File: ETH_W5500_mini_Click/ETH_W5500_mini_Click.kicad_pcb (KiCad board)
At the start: 2 copper layers, 25.4 x 42.9 mm, 8 parts, among them J1 ETH W5500 mini Click v1.0, M1 W5500-MINI

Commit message: project files updated to Kicad version 9.0.1
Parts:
- J1: value ETH W5500 mini Click v1.0 -> ETH W5500 mini Click v${REVISION}

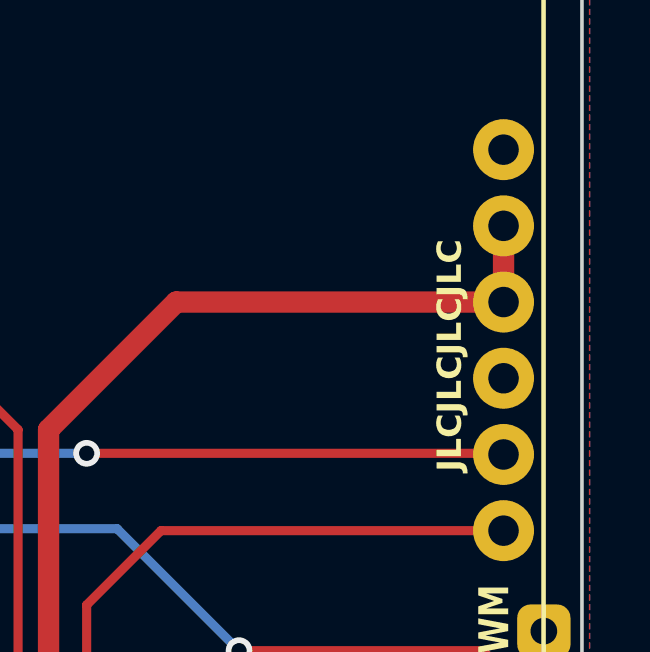
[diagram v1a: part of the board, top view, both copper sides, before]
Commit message: updated 3D models and project files
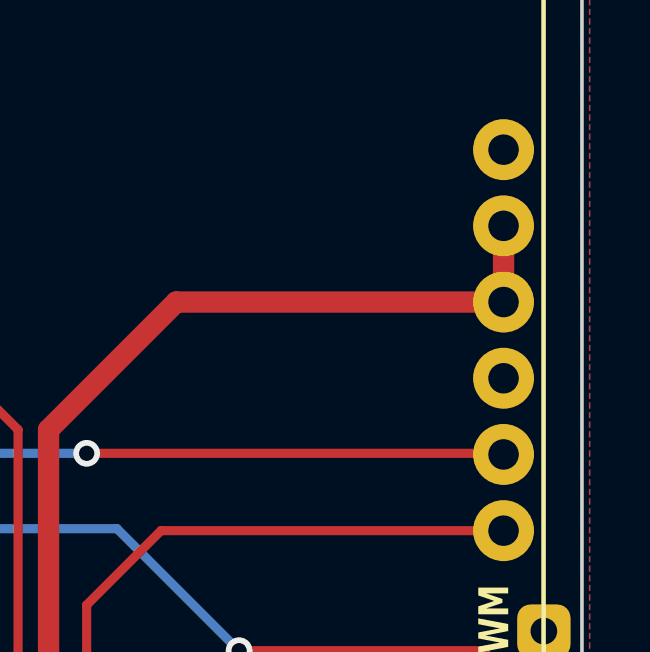
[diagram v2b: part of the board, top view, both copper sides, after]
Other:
- board text removed: "JLCJLCJLCJLC"
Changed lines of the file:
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@@
 		)
 		(embedded_fonts no)
-		(model "${KIPRJMOD}/shapes3D/USR-ES1 Ethernet Module.stp"
+		(model "${KIPRJMOD}/shapes3D/USR-ES1 Ethernet Module.stpZ"
 			(offset
 				(xyz -1.27 -19.05 6.985)
@@
 		)
 	)
-	(gr_text "JLCJLCJLCJLC"
-		(at 113.538 58.42 90)
-		(layer "F.SilkS")
-		(effects
-			(font
-				(size 0.81 0.81)
-				(thickness 0.15)
-				(bold yes)
-			)
-			(justify left bottom)
-		)
-	)
 	(gr_text "Designed by MPro"
 		(at 114.173 84.709 0)
@@
 			(prefix "")
 			(suffix "")
-			(units 3)
+			(units 2)
 			(units_format 1)
-			(precision 4)
+			(precision 2)
 		)
 		(style
@@
 			(keep_text_aligned yes)
 		)
-		(gr_text "25,4000 mm"
+		(gr_text "25.40 mm"
 			(at 104.775 36.95 0)
 			(layer "Dwgs.User")
@@
 			(prefix "")
 			(suffix "")
-			(units 3)
+			(units 2)
 			(units_format 1)
-			(precision 4)
+			(precision 2)
 		)
 		(style
@@
 			(keep_text_aligned yes)
 		)
-		(gr_text "42,9260 mm"
+		(gr_text "42.93 mm"
 			(at 87.75 63.8648 90)
 			(layer "Dwgs.User")
@@
 			(prefix "")
 			(suffix "")
-			(units 3)
+			(units 2)
 			(units_format 1)
-			(precision 4)
+			(precision 2)
 		)
 		(style
@@
 			(keep_text_aligned yes)
 		)
-		(gr_text "22,8600 mm"
+		(gr_text "22.86 mm"
 			(at 103.505 87.75 0)
 			(layer "Dwgs.User")
